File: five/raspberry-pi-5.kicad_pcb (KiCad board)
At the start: 4 copper layers, 85 x 56 mm, 47 parts, among them J101 DX07S016JA3, J202 G85D1171012HHR, SW101 SKSG, U101 TPM_Infineon_SLB9670, U501 TPSM33625

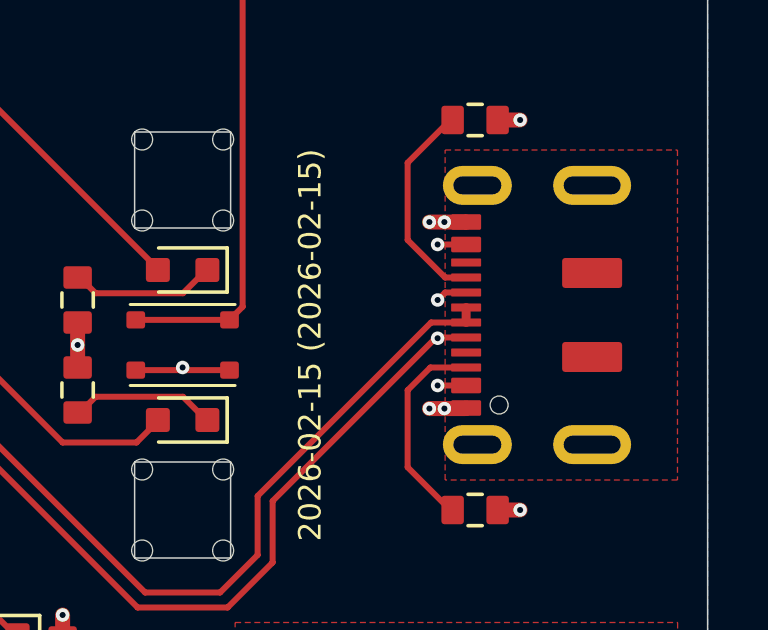
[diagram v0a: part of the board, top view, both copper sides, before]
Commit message: KiCad 10
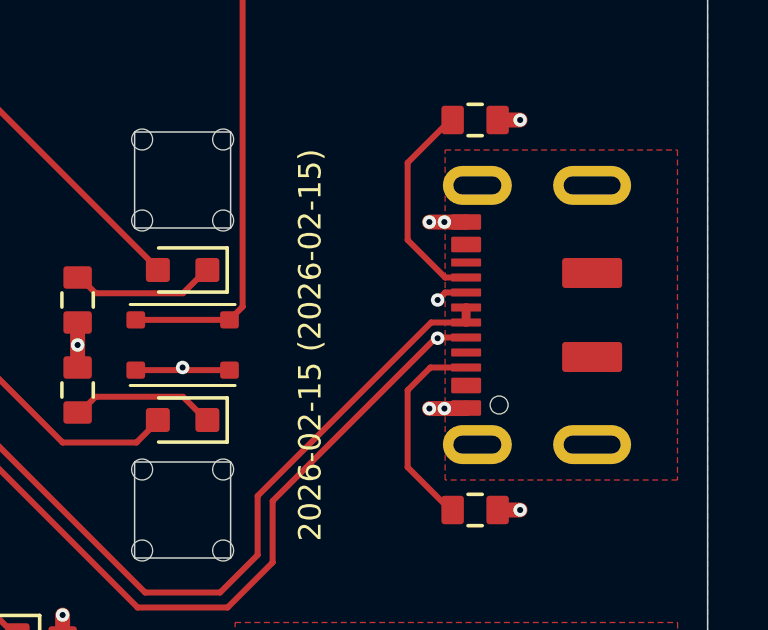
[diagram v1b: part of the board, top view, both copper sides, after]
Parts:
- C503, C505: value 10u -> 22u
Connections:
- net Shield renamed /M2 Connector/Shield
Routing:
- net unconnected-(J101-VBUS-PadV): track 7.40 -> 0.00 mm, vias 2 -> 0
